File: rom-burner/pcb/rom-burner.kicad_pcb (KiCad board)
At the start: 2 copper layers, 88.9 x 55.9 mm, 11 parts, among them U1 74HC595, U2 74HC595, U3 SST39SF010/20/40, U4 74HC595, U5 4021, U6 Arduino_Uno_shield

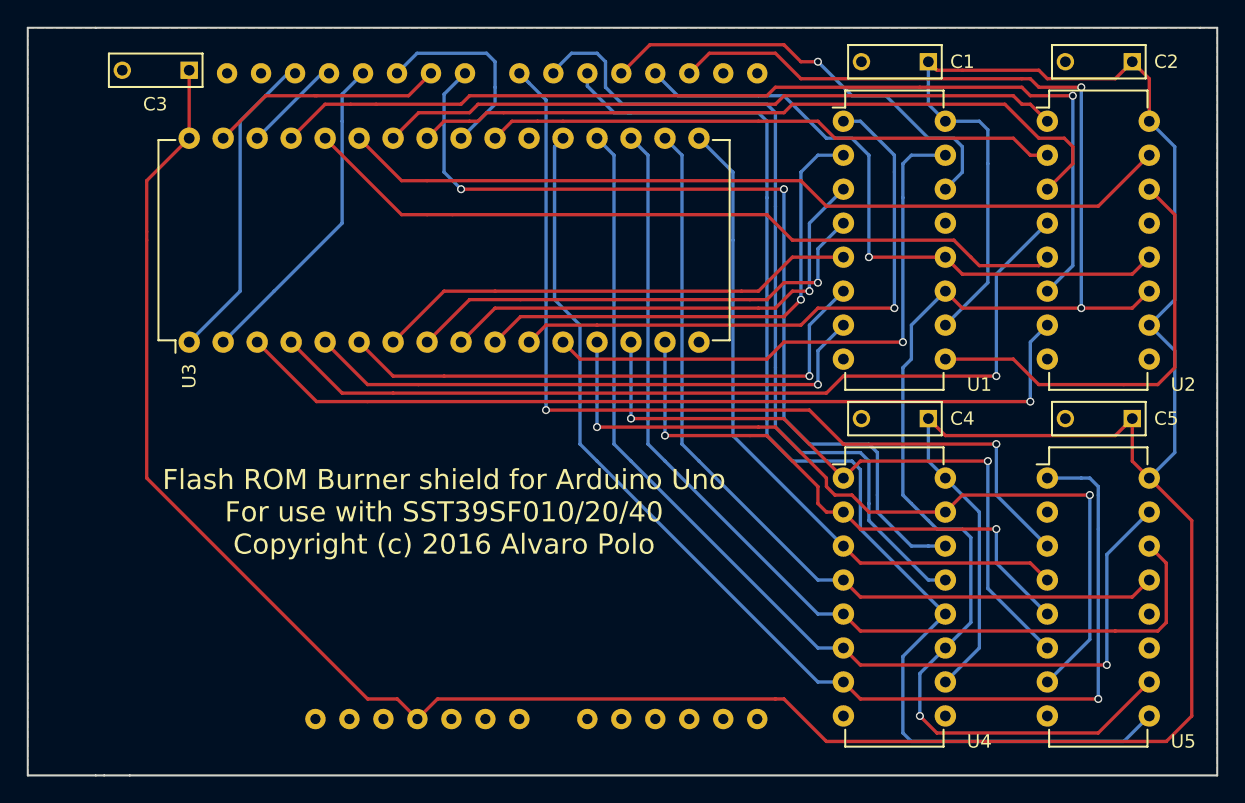
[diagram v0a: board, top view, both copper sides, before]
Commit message: upd: rom-burner migrated to KiCAD 6
- Removed redundant traces
- Fixed bad connections
- Removed all Warnings
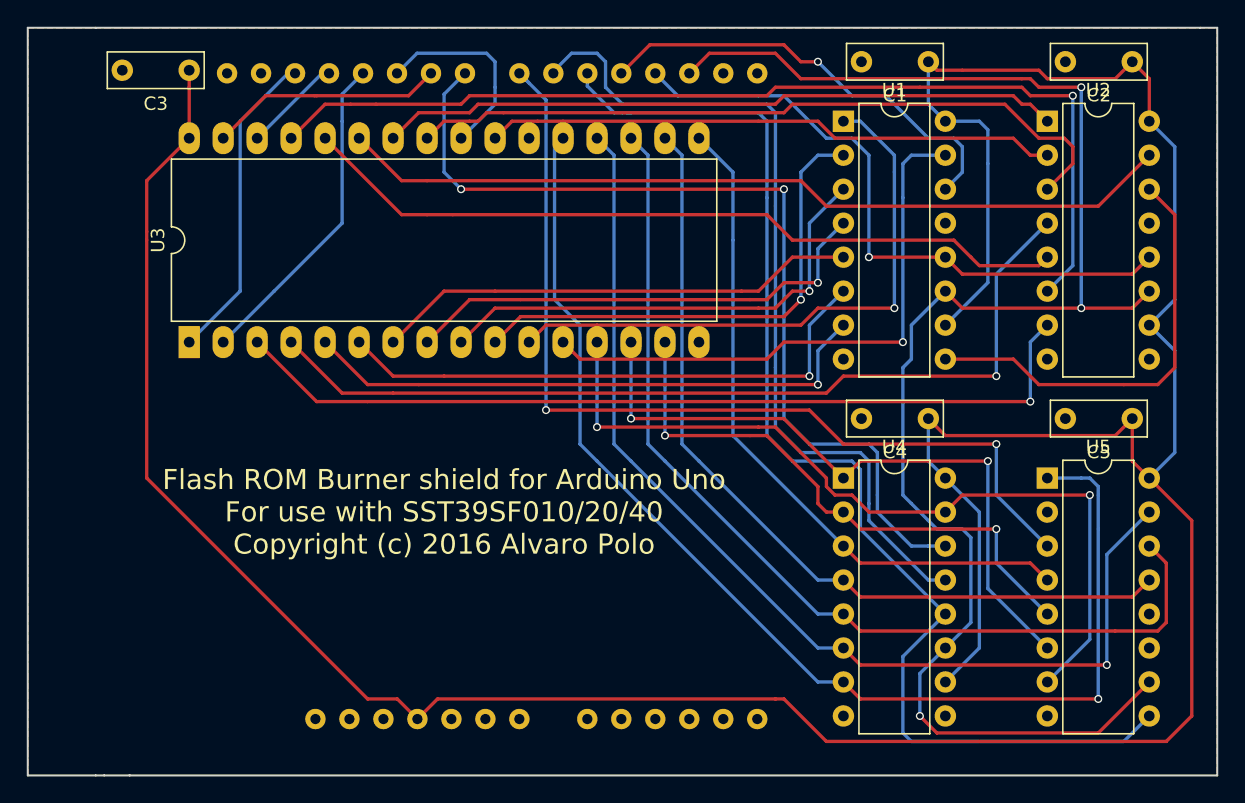
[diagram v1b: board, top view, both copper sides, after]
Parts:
- C1, C2, C3, C4, C5: footprint Capacitors_ThroughHole:C_Rect_L7_W2.5_P5 -> Capacitor_THT:C_Rect_L7.0mm_W2.5mm_P5.00mm
- U1, U2, U4, U5: footprint Housings_DIP:DIP-16_W7.62mm -> Package_DIP:DIP-16_W7.62mm
- U3: value SST39SF010/20/40 -> SST39SF040; footprint Housings_DIP:DIP-32_W15.24mm -> Package_DIP:DIP-32_W15.24mm_LongPads
- U6: footprint arduino_uno_shield -> Arduino:arduino_uno_shield
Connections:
- C1 pad 2: GND -> Net-(C1-Pad2)
- C2 pad 2: GND -> Net-(C2-Pad2)
- C4 pad 2: GND -> Net-(C4-Pad2)
- U1 pad 16: VCC -> Net-(C1-Pad2)
- U2 pad 16: VCC -> Net-(C2-Pad2)
- U2 pad 9: Net-(U2-Pad9) -> unconnected-(U2-Pad9)
- U4 pad 16: VCC -> Net-(C4-Pad2)
- U4 pad 9: Net-(U4-Pad9) -> unconnected-(U4-Pad9)
- U5 pad 11: Net-(U5-Pad11) -> unconnected-(U5-Pad11)
- U5 pad 12: Net-(U5-Pad12) -> unconnected-(U5-Pad12)
- U5 pad 2: Net-(U5-Pad2) -> unconnected-(U5-Pad2)
- U6 pad 1: Net-(U6-Pad1) -> unconnected-(U6-Pad1)
- U6 pad 15: Net-(U6-Pad15) -> unconnected-(U6-Pad15)
- U6 pad 16: Net-(U6-Pad16) -> unconnected-(U6-Pad16)
- U6 pad 17: Net-(U6-Pad17) -> unconnected-(U6-Pad17)
- U6 pad 18: Net-(U6-Pad18) -> unconnected-(U6-Pad18)
- U6 pad 19: Net-(U6-Pad19) -> unconnected-(U6-Pad19)
- U6 pad 2: Net-(U6-Pad2) -> unconnected-(U6-Pad2)
- U6 pad 22: Net-(U6-Pad22) -> unconnected-(U6-Pad22)
- U6 pad 23: Net-(U6-Pad23) -> unconnected-(U6-Pad23)
- U6 pad 24: Net-(U6-Pad24) -> unconnected-(U6-Pad24)
- U6 pad 25: Net-(U6-Pad25) -> unconnected-(U6-Pad25)
- U6 pad 26: Net-(U6-Pad26) -> unconnected-(U6-Pad26)
- U6 pad 27: Net-(U6-Pad27) -> unconnected-(U6-Pad27)
- U6 pad 28: Net-(U6-Pad28) -> unconnected-(U6-Pad28)
- U6 pad 29: Net-(U6-Pad29) -> unconnected-(U6-Pad29)
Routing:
- net /DQ3: track 51.2 -> 402.4 mm, vias 0 -> 2
- net /DQ0: track 62.0 -> 243.7 mm, vias 2 -> 8
- net /DQ7: track 90.5 -> 0.00 mm, vias 1 -> 0
- net /DQ6: track 79.8 -> 0.00 mm, vias 1 -> 0
- net /DQ5: track 74.4 -> 0.00 mm
- net /DQ4: track 63.6 -> 0.00 mm
- net /A11: track 54.6 -> 0.00 mm
- net OE: track 15.0 -> 69.6 mm
- net /DQ1: track 50.6 -> 0.00 mm, vias 2 -> 0
- net /A1: track 44.6 -> 0.00 mm, vias 1 -> 0
- net /DQ2: track 43.3 -> 0.00 mm, vias 2 -> 0
- net /A0: track 43.2 -> 0.00 mm, vias 1 -> 0
- net /A10: track 42.9 -> 0.00 mm
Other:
- net class Default removed

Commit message: fix: additional fixes to rom-burner pcb
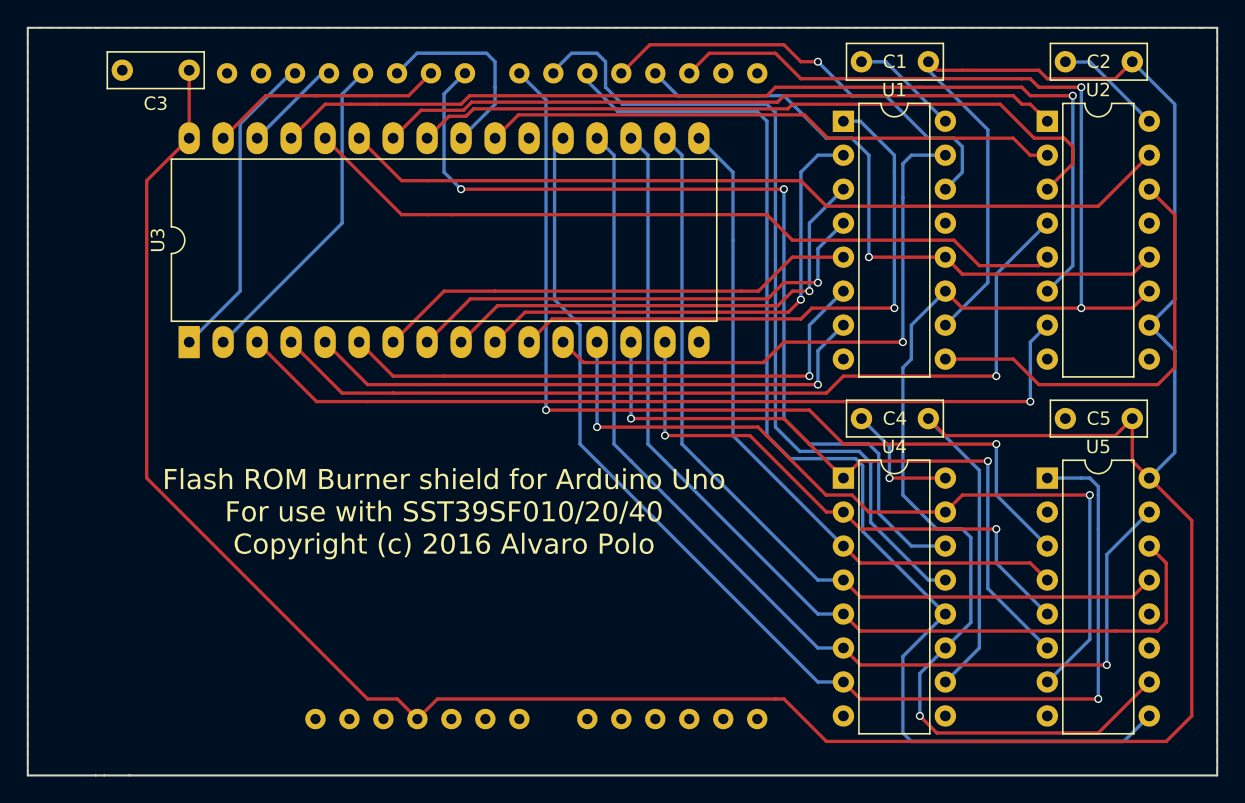
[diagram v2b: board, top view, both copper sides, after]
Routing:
- net /DQ3: track 402.4 -> 51.2 mm, vias 2 -> 0
- net /DQ0: track 243.7 -> 61.6 mm, vias 8 -> 2
- net /DQ7: track 0.00 -> 90.5 mm, vias 0 -> 1
- net /DQ6: track 0.00 -> 79.8 mm, vias 0 -> 1
- net /DQ5: track 0.00 -> 74.4 mm
- net /DQ4: track 0.00 -> 63.6 mm
- net OE: track 69.6 -> 15.0 mm
- net /A11: track 0.00 -> 54.6 mm
- net /DQ1: track 0.00 -> 50.6 mm, vias 0 -> 2
- net /A1: track 0.00 -> 44.6 mm, vias 0 -> 1
- net /A0: track 0.00 -> 43.4 mm, vias 0 -> 1
- net /A10: track 0.00 -> 43.2 mm
- net /DQ2: track 0.00 -> 42.6 mm, vias 0 -> 2
- net Net-(C4-Pad2): track 0.00 -> 9.50 mm, vias 0 -> 1
- net Net-(C1-Pad2): track 0.00 -> 8.11 mm
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
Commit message: upd: update PCB designs to KiCAD 8
- rom-burner: Update libraries
- rom-burner: Re-routed some paths to improve thermal reliefs in GND
  pads and avoid isolated islands
- rom64kb: Re-routed some paths to avoid isolated islands
- rom64kb: Removed solder mask in golden fingers area
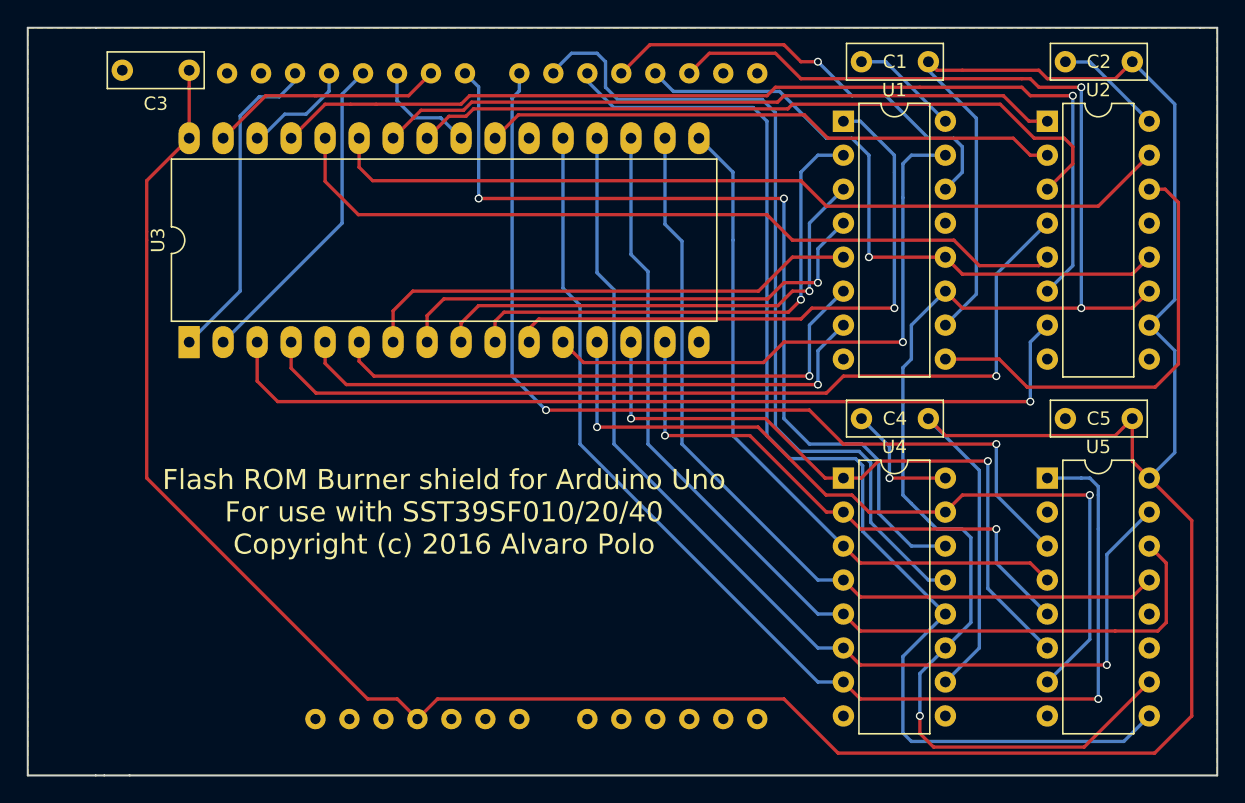
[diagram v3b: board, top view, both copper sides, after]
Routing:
- net OE: track 15.0 -> 8.00 mm
- net DATA_OUT: track 69.7 -> 67.4 mm
- net /A13: track 58.2 -> 60.1 mm
- net /A15: track 65.9 -> 67.6 mm
- net CLOCK: track 120.9 -> 122.5 mm
- net /A5: track 36.3 -> 37.7 mm
- net /A8: track 62.7 -> 64.0 mm
- net /A4: track 36.3 -> 37.4 mm
- net /A12: track 67.8 -> 69.0 mm
- net Net-(U1-Pad9): track 32.6 -> 33.7 mm
- net /A7: track 43.4 -> 44.3 mm
- net /A2: track 37.4 -> 38.3 mm
- net /A6: track 42.1 -> 42.9 mm
- net /A3: track 36.3 -> 37.1 mm
- net ADDR17: track 7.38 -> 8.17 mm
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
